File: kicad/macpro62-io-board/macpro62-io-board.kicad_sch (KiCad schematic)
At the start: 387 parts, among them J1 IOB-HS1 MCIO 124 RA <- CB J3, J11 USB-C C1 receptacle vertical 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, J12 USB-C C2 receptacle vertical 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, J13 USB-C C3 receptacle vertical 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, J14 USB-C C4 receptacle vertical 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, J15 USB-C C5 receptacle vertical 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, J16 USB-C C6 receptacle vertical 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, J2 DISPLAY-LINK MCIO 74 RA <- Fa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, J21 USB 3.2 Gen2 Std-A vertical A1, J22 USB 3.2 Gen2 Std-A vertical A2, J23 USB 3.2 Gen2 Std-A vertical A3, J24 USB 3.2 Gen2 Std-A vertical A4, J25 RJ45 vertical magjack 2.5G (E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, J26 DNP rev A: RJ45 10G magjack s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, J27 HDMI type A vertical, J28 Stock audio module connector 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, J29 Speaker 2P JST SH vertical (s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, J3 Stock PSU DC-out 12P (PROVISI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, J30 OPTIONAL 2P: stock I/O-wall b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, J31 I/O-wall flex ZIF 14P 0.5 (st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, J4 Stock PSU signal 6P (PROVISIO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, J5 Micro-Fit 2x4 -> BP J2 (1-2 1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, J6 IOB-LINK GH15 vertical <- BP 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, SW1 Power button PTS810 on the IO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, SW2 DIAG button TL3342 (back side), U1 TPS65994AD PD #1 (C1, C2), U11 TUSB1046A-DCI C1 mux/redriver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, U12 TUSB1046A-DCI C2 mux/redriver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, U13 TUSB1046A-DCI C3 mux/redriver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, U14 TUSB1046A-DCI C4 mux/redriver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, U15 TUSB1046A-DCI C5 mux/redriver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, U16 TUSB1046A-DCI C6 mux/redriver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, U2 TPS65994AD PD #2 (C3, C4), U21 TUSB1002A A1 redriver, U22 TUSB1002A A2 redriver, U23 TUSB1002A A3 redriver, U24 TUSB1002A A4 redriver, U25 SY6280AAC / TPS2553 1.5 A swi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, U26 SY6280AAC / TPS2553 1.5 A swi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, U27 SY6280AAC / TPS2553 1.5 A swi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, U28 SY6280AAC / TPS2553 1.5 A swi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, U3 TPS65994AD PD #3 (C5, C6), U30 DRV5032FB (OD, 5 Hz low power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, U31 DRV5032FB (OD, 5 Hz low power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, U32 CH334R H1b <- H1a port 4, U33 CH334R H2 <- IOB-LINK USB2 (B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, U34 CH334R H1a <- HS1 USB2 (CB PC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, U4 W25Q80DV class 8 Mbit (PD #1 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, U40 TPS259824ONRGER eFuse 12 V (I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, U41 TPS56C215RNNR 5V_C buck 12 A, U42 TPS56C215RNNR 5V_A buck 12 A, U43 TLV62585DRL 3V3 3 A from 5V_A, U50 Intel i226-V 2.5GbE, U51 i226 NVM 2 Mbit+ SPI flash (I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, U6 W25Q80DV class 8 Mbit (PD #2 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, U60 TDP158RSBR HDMI retimer, U61 TLV75511PDBV 1.1 V LDO (TDP15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, U7 W25Q80DV class 8 Mbit (PD #3 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, U70 CM108B USB audio codec (UAC1), U71 PAM8302AAS 2.5 W mono class-D, U80 TLC59116IPWR @0x60 (A3..A0 = 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, U81 LIS2DH12TR @0x18 (optional ro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, U82 BL24C64A-SFRC IOB ID EEPROM @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, U83 TCA9517DGKR I2C buffer: I2C_S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, U84 74LVC1G07 PD_INT_N -> IOB_INT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, Y1 12MHz 3225 +/-20ppm, Y2 12MHz 3225 +/-20ppm, Y3 12MHz 3225 +/-20ppm, Y4 25MHz 3225 +/-30ppm (i226), Y5 12MHz 3225 (CM108B)

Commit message: I/O board: second 2.5GbE (2x i226-V, HR913790A set back), ETH2 plate opening, CPU link pinout v0.2
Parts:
- removed J25: RJ45 vertical magjack 2.5G (ETH1, Xb 63.5), MP62_IO:MP62_RJ45_Mag_2G5_Vertical_PLACEHOLDER, symbol MP62_IO:RJ45_MAG
- removed J26: DNP rev A: RJ45 10G magjack site (rev B AQC107 vi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, MP62_IO:MP62_RJ45_Mag_2G5_Vertical_PLACEHOLDER, symbol MP62_IO:RJ45_MAG
- added C284: 100nF, MP62_IO:C_0402_1005Metric, symbol MP62_IO:C
- added C285: 100nF (CB keeps 1uF + 0.1uF + diode-OR with 3V3_D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, MP62_IO:C_0402_1005Metric, symbol MP62_IO:C
- added C286: dVdt (inrush <= 2 A, value per datasheet), MP62_IO:C_0402_1005Metric, symbol MP62_IO:C
- added C287, C290: 100nF BOOT, MP62_IO:C_0402_1005Metric, symbol MP62_IO:C
- added C288, C291: 4.7uF VREG5, MP62_IO:C_0402_1005Metric, symbol MP62_IO:C
- added C289, C292: SS (value per datasheet), MP62_IO:C_0402_1005Metric, symbol MP62_IO:C
- added C293, C294: 22uF 0805, MP62_IO:C_0402_1005Metric, symbol MP62_IO:C
- added C295: 10uF 0805, MP62_IO:C_0402_1005Metric, symbol MP62_IO:C
- added C296: 10uF 0402, MP62_IO:C_0402_1005Metric, symbol MP62_IO:C
- added J25: HanRun HR913790A vertical 2.5G magjack (ETH1), MP62_IO:MP62_RJ45_HanRun_HR913790A_Vertical_2G5, symbol MP62_IO:RJ45_HR913790A
- added J26: HanRun HR913790A vertical 2.5G magjack (ETH2), MP62_IO:MP62_RJ45_HanRun_HR913790A_Vertical_2G5, symbol MP62_IO:RJ45_HR913790A
- added L45: i226 #2 SVR inductor (value per Intel design guid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, MP62_IO:L_1008_2520Metric, symbol MP62_IO:L
- added R186: FB top (5.10 V), MP62_IO:R_0402_1005Metric, symbol MP62_IO:R
- added R187, R190: FB bottom, MP62_IO:R_0402_1005Metric, symbol MP62_IO:R
- added R188: 10k PG pull-up, MP62_IO:R_0402_1005Metric, symbol MP62_IO:R
- added R189: FB top (3.3 V), MP62_IO:R_0402_1005Metric, symbol MP62_IO:R
- added R191: 10k, MP62_IO:R_0402_1005Metric, symbol MP62_IO:R
- added U52: Intel i226-V 2.5GbE #2 (HS1 k14, PCH RP4 / HSIO 1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, MP62_IO:MP62_Intel_i226V_QFN-56_7x7_P0.4_PLACEHOLDER, symbol MP62_IO:I226V
- added U53: i226 #2 NVM 2 Mbit+ SPI flash (Intel image), MP62_IO:SOIC-8_3.9x4.9mm_P1.27mm, symbol MP62_IO:SPI_FLASH
- added Y6: 25MHz 3225 +/-30ppm (i226 #2), MP62_IO:Crystal_SMD_3225-4Pin_3.2x2.5mm, symbol MP62_IO:XTAL4
- C244, C256: value 10uF 0402 -> 100nF 0402 (magjack common centre tap)
- C245, C246: value 100nF -> 220nF 0201 X7R (i226 TX -> PCH RX AC cap)
- C247: value 10uF 0402 -> 18pF
- C248: value 100nF -> 18pF
- C249: value 22pF -> 22uF 0603
- C250: value 22pF -> 1uF
- C251: value 4.7uF -> 100nF
- C252: value 100nF -> 22uF 0603
- C253: value 10uF 0402 -> 1uF
- C255, C283: value 10uF 0402 -> 100nF
- C257: value 100nF (L into IN+) -> 10uF 0402
- C258: value 100nF (R into IN+, mono sum) -> 100nF
- C259: value 220nF (IN- to AGND) -> 100nF
- C260: value 10uF 0603 -> 10uF 0402
- C261: value 1uF -> 100nF
- C262: value 10uF 1206 25V (header) -> 22pF
- C263: value 100nF (debounce; pull-up on BP) -> 22pF
- C264: value 100nF -> 4.7uF
- C266: value 1uF -> 10uF 0402
- C268, C269: value 100nF -> 10uF 0402
- C270: value 100nF -> 100nF (L into IN+)
- C271: value 100nF -> 100nF (R into IN+, mono sum)
- C272: value 100nF (CB keeps 1uF + 0.1uF + diode-OR with 3V3_DSW) -> 220nF (IN- to AGND)
- C273: value dVdt (inrush <= 2 A, value per datasheet) -> 10uF 0603
- C274: value 100nF BOOT -> 1uF
- C275: value 4.7uF VREG5 -> 10uF 1206 25V (header)
- C276: value SS (value per datasheet) -> 100nF (debounce; pull-up on BP)
- C277: value 100nF BOOT -> 100nF
- C278: value 4.7uF VREG5 -> 100nF
- C279: value SS (value per datasheet) -> 1uF
- C280, C281: value 22uF 0805 -> 100nF
- C282: value 10uF 0805 -> 100nF
- L44: value i226 SVR inductor (value per Intel design guide) -> i226 #1 SVR inductor (value per Intel design guide)
- R132: value 10k (DNP if CB pulls up) -> 330R (green link LED; orange half of the bicolour unused); now fitted; now in the parts list
- R133: value 1.8k DDC pull-up (sink side) -> 330R (yellow activity LED)
- R134: value 1.8k DDC pull-up (sink side) -> 10k (DNP if CB pulls up); now not fitted; now left out of the parts list
- R135: value 100k HPD pull-down -> RSET (value per Intel)
- R136: value 100k -> 330R (green link LED; orange half of the bicolour unused)
- R137: value 10k (L+R mix into the mono ADC; CM6646 upgrade = stereo line in) -> 330R (yellow activity LED)
- R138: value 10k -> 10k (DNP if CB pulls up); now not fitted; now left out of the parts list
- R139: value DNP 2.2k (only if the stock line-in jack is a mic/combo) -> 1.8k DDC pull-up (sink side); now fitted; now in the parts list
- R140: value 100k jack-detect pull-up -> 1.8k DDC pull-up (sink side)
- R141: value 100k jack-detect pull-up -> 100k HPD pull-down
- R142: value 0R (optical TX/RX module supply; 10R if the module wants filtering) -> 100k
- R143: value DNP: optical input not supported by CM108B (CM6646 upgrade) -> 10k (L+R mix into the mono ADC; CM6646 upgrade = stereo line in); now fitted; now in the parts list
- R144: value 100k (amp off until codec GPIO3 enables; firmware mutes on JD_HP) -> 10k
- R145: value DNP 0R (only if J4 5/6 prove to be 3.3 V SMBus) -> DNP 2.2k (only if the stock line-in jack is a mic/combo)
- R146: value DNP 0R -> 100k jack-detect pull-up; now fitted; now in the parts list
- R147: value DNP 0R: GND? (probe) -> 100k jack-detect pull-up; now fitted; now in the parts list
- R148: value DNP 0R: GND? (probe) -> 0R (optical TX/RX module supply; 10R if the module wants filtering); now fitted; now in the parts list
- R149: value 0R: community claim pins 3+6 = power button -> DNP: optical input not supported by CM108B (CM6646 upgrade); now not fitted; now left out of the parts list
- R150: value DNP 0R: LED-MCU logic 3V3? (probe) -> 100k (amp off until codec GPIO3 enables; firmware mutes on JD_HP); now fitted; now in the parts list
- R151: value DNP 0R: 3V3? (probe) -> DNP 0R (only if J4 5/6 prove to be 3.3 V SMBus)
- R152: value 0R: button return (pins 3+6) -> DNP 0R; now not fitted; now left out of the parts list
- R153: value DNP 0R: LED-MCU I2C SCL? (probe; must be 3.3 V) -> DNP 0R: GND? (probe)
- R154: value DNP 0R: LED-MCU I2C SDA? (probe) -> DNP 0R: GND? (probe)
- R155: value DNP 0R: flex IRQ/motion? (probe) -> 0R: community claim pins 3+6 = power button; now fitted; now in the parts list
- R156: value DNP 0R: LED supply 5 V? (probe; S0 only) -> DNP 0R: LED-MCU logic 3V3? (probe)
- R157: value DNP 0R: GND? (probe) -> DNP 0R: 3V3? (probe)
- R158: value DNP 0R: 3V3? (probe) -> 0R: button return (pins 3+6); now fitted; now in the parts list
- R159: value DNP 0R: GND? (probe) -> DNP 0R: LED-MCU I2C SCL? (probe; must be 3.3 V)
- R160: value DNP 0R: GND? (probe) -> DNP 0R: LED-MCU I2C SDA? (probe)
- R161: value 10k (read via PD #1 GPIO2; S0 only) -> DNP 0R: flex IRQ/motion? (probe); now not fitted; now left out of the parts list
- R162: value REXT ~ 2.7k (Iout ~ 7 mA max; PWM per channel) -> DNP 0R: LED supply 5 V? (probe; S0 only); now not fitted; now left out of the parts list
- R163: value 10k (write-protect by default) -> DNP 0R: GND? (probe); now not fitted; now left out of the parts list
- R164: value DNP 0R (program) -> DNP 0R: 3V3? (probe)
- R165, R166: value 4.7k -> DNP 0R: GND? (probe); now not fitted; now left out of the parts list
- R167: value 10k (DNP if the BP pulls up) -> 10k (read via PD #1 GPIO2; S0 only); now fitted; now in the parts list
- R168: value UVLO top (~10.5 V on) -> REXT ~ 2.7k (Iout ~ 7 mA max; PWM per channel)
- R169: value UVLO bottom -> 10k (write-protect by default)
- R170: value ILIM ~10 A (value per datasheet) -> DNP 0R (program); now not fitted; now left out of the parts list
- R171: value IMON (value per datasheet) -> 4.7k
- R172: value 10k -> 4.7k
- R173: value 10k -> 10k (DNP if the BP pulls up); now not fitted; now left out of the parts list
- R174: value 0R (fault -> IOB_INT_N, OD) -> UVLO top (~10.5 V on)
- R175: value MODE strap (FCCM, 800 kHz) -> UVLO bottom
- R176: value FB top (5.10 V) -> ILIM ~10 A (value per datasheet)
- R177: value FB bottom -> IMON (value per datasheet)
- R178: value 10k PG pull-up -> 10k
- R179: value MODE strap (FCCM, 800 kHz) -> 10k
- R180: value FB top (5.10 V) -> 0R (fault -> IOB_INT_N, OD)
- R181: value FB bottom -> MODE strap (FCCM, 800 kHz)
- R182: value 10k PG pull-up -> FB top (5.10 V)
- R183: value FB top (3.3 V) -> FB bottom
- R184: value FB bottom -> 10k PG pull-up
- R185: value 10k -> MODE strap (FCCM, 800 kHz)
- U50: value Intel i226-V 2.5GbE -> Intel i226-V 2.5GbE #1 (HS1 k10, PCH RP3 / HSIO 12, CLKOUT_SRC12)
- U51: value i226 NVM 2 Mbit+ SPI flash (Intel image) -> i226 #1 NVM 2 Mbit+ SPI flash (Intel image)
- Y4: value 25MHz 3225 +/-30ppm (i226) -> 25MHz 3225 +/-30ppm (i226 #1)
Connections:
- net +12V_MAIN: now also C275.1, R174.1; no longer C262.1, R168.1
- net 1V1_HDMI: now also C257.1, C258.1, C259.1; no longer C244.1, C245.1, C246.1
- net 3V3: now also C252.1, C253.1, C254.1, C255.1, C260.1, C261.1, R133.2, R134.2, R136.2, R137.2, R138.2, R148.1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; no longer C247.1, C248.1, C271.1, C280.1, C281.1, R142.1, R158.2, R161.2, R165.2, R166.2, R183.1
- net 3V3_SB: now also C277.1, C278.1, C279.1, C280.1, C281.1, C282.1, R156.2, R157.2, R169.2, R179.2, R184.2, C296.1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; no longer C264.1, C265.1, C266.1, C267.1, C268.1, C269.1, C270.1, R150.2, R151.2, R163.2, R167.2, R172.2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
- net 5V_A: now also C268.1, C273.1, C274.1, R162.2, C295.1, R186.1; no longer C255.1, C260.1, C261.1, C282.1, R156.2, R180.1
- net 5V_C: now also R182.1; no longer R176.1
- net AGND: now also C272.2; no longer C259.2
- net AMP_INN: now also C272.1; no longer C259.1
- net AMP_INP: now also C270.2, C271.2; no longer C257.2, C258.2
- net AMP_SD#: now also R150.1; no longer R144.1
- net AUD_3V3: now also C264.1, C265.1, R146.2, R147.2; no longer C251.1, C252.1, R140.2, R141.2
- net AUD_AVDD: now also C266.1, C267.1; no longer C253.1, C254.1
- net AUD_OPT_3V3: now also C269.1, R148.2; no longer C256.1, R142.2
- net AUD_XI: now also C262.1; no longer C249.1
- net AUD_XO: now also C263.1; no longer C250.1
- net BK3_FB: now also R189.2, R190.1; no longer R183.2, R184.1
- net BKA_BOOT: now also C290.1; no longer C277.1
- net BKA_FB: now also R186.2, R187.1; no longer R180.2, R181.1
- net BKA_MODE: now also R185.1; no longer R179.1
- net BKA_SS: now also C292.1; no longer C279.1
- net BKA_SW: now also C290.2; no longer C277.2
- net BKA_VREG5: now also C291.1; no longer C278.1
- net BKC_BOOT: now also C287.1; no longer C274.1
- net BKC_FB: now also R182.2, R183.1; no longer R176.2, R177.1
- net BKC_MODE: now also R181.1; no longer R175.1
- net BKC_SS: now also C289.1; no longer C276.1
- net BKC_SW: now also C287.2; no longer C274.2
- net BKC_VREG5: now also C288.1; no longer C275.1
- net DIAG_BTN_N: now also R167.1; no longer R161.1
- net DL_HPD2: now also R142.1; no longer R136.1
- net EFUSE_DVDT: now also C286.1; no longer C273.1
- net EFUSE_EN: now also R174.2, R175.1; no longer R168.2, R169.1
- net EFUSE_FLT#: now also R179.1, R180.1; no longer R173.1, R174.1
- net EFUSE_ILIM: now also R176.1; no longer R170.1
- net EFUSE_IMON: now also R177.1; no longer R171.1
- net EFUSE_PG: now also R178.1; no longer R172.1
- net ETH1_LED_ACT#: now also J25.13 (LEDY_K)
- net ETH1_LED_LINK#: now also J25.11 (LEDGO_11)
- net ETH1_MDI0_N: now also J25.3 (TRD1-)
- net ETH1_MDI0_P: now also J25.2 (TRD1+)
- net ETH1_MDI1_N: now also J25.5 (TRD2-)
- net ETH1_MDI1_P: now also J25.4 (TRD2+)
- net ETH1_MDI2_N: now also J25.7 (TRD3-)
- net ETH1_MDI2_P: now also J25.6 (TRD3+)
- net ETH1_MDI3_N: now also J25.9 (TRD4-)
- net ETH1_MDI3_P: now also J25.8 (TRD4+)
- net GND: now also C257.2, C258.2, C259.2, C274.2, C277.2, R141.2, R142.2, R149.2, R150.2, R153.2, R154.2, R158.2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; no longer C245.2, C246.2, C270.2, C271.2, C272.2, R136.2, R143.2, R144.2, R147.2, R148.2, R152.2, R157.2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
- net HDMI_5V_OUT: now also R139.2, R140.2; no longer R133.2, R134.2
- net HDMI_HPD: now also R141.1; no longer R135.1
- net HDMI_SCL: now also R139.1; no longer R133.1
- net HDMI_SDA: now also R140.1; no longer R134.1
- net HP_L: now also C270.1; no longer C257.1
- net HP_R: now also C271.1; no longer C258.1
- net I226_CLKREQ#: now also R134.1; no longer R132.1
- net I226_PERST#: now also U52.7 (PERST#)
- net I226_WAKE#: now also U52.9 (WAKE#)
- net I2C_PD_SCL: now also R171.1; no longer R165.1
- net I2C_PD_SDA: now also R172.1; no longer R166.1
- net I2C_SYS_SCL: now also R151.2, R159.2; no longer R145.2, R153.2
- net I2C_SYS_SDA: now also R152.2, R160.2; no longer R146.2, R154.2
- net IOB_EE_WP: now also R169.1, R170.1; no longer R163.1, R164.1
- net IOB_INT_N: now also R161.2, R173.1, R180.2; no longer R155.2, R167.1, R174.2
- net JD_HP: now also R146.1; no longer R140.1
- net JD_LINE: now also R147.1; no longer R141.1
- net LED_REXT: now also R168.1; no longer R162.1
- net LINE_IN_MONO: now also R143.2, R144.2, R145.2; no longer R137.2, R138.2, R139.2
- net LINE_L: now also R143.1; no longer R137.1
- net LINE_R: now also R144.1; no longer R138.1
- net MIC_BIAS: now also R145.1; no longer R139.1
- net PG_3V3: now also R191.1; no longer R185.1
- net PG_5VA: now also R188.1; no longer R182.1
- net PG_5VC: now also R184.1; no longer R178.1
- net PSU_SMB_CLK: now also R151.1; no longer R145.1
- net PSU_SMB_DAT: now also R152.1; no longer R146.1
- net PWRBTN_IN_N: now also C276.1, R155.2; no longer C263.1, R149.2
- net SPDIF_RX: now also R149.1; no longer R143.1
- net VBAT_RTC: now also C285.1; no longer C272.1
- net WALL_P1: now also R153.1; no longer R147.1
- net WALL_P10: now also R162.1; no longer R156.1
- net WALL_P11: now also R163.1; no longer R157.1
- net WALL_P12: now also R164.1; no longer R158.1
- net WALL_P13: now also R165.1; no longer R159.1
- net WALL_P14: now also R166.1; no longer R160.1
- net WALL_P2: now also R154.1; no longer R148.1
- net WALL_P3: now also R155.1; no longer R149.1
- new net ETH1_CT: C244.1, J25.1 (CT)
- new net ETH1_LEDG_A: J25.12 (LEDGO_12), R132.1
- new net ETH1_LEDY_A: J25.14 (LEDY_A), R133.1
- new net ETH2_CT: C256.1, J26.1 (CT)
- new net ETH2_LEDG_A: J26.12 (LEDGO_12), R136.1
- new net ETH2_LEDY_A: J26.14 (LEDY_A), R137.1
- new net ETH2_LED_ACT#: J26.13 (LEDY_K), U52.29 (LED1#)
- new net ETH2_LED_LINK#: J26.11 (LEDGO_11), U52.28 (LED0#)
- new net ETH2_MDI0_N: J26.3 (TRD1-), U52.21 (MDI0N)
- new net ETH2_MDI0_P: J26.2 (TRD1+), U52.20 (MDI0P)
- new net ETH2_MDI1_N: J26.5 (TRD2-), U52.23 (MDI1N)
- new net ETH2_MDI1_P: J26.4 (TRD2+), U52.22 (MDI1P)
- new net ETH2_MDI2_N: J26.7 (TRD3-), U52.25 (MDI2N)
- new net ETH2_MDI2_P: J26.6 (TRD3+), U52.24 (MDI2P)
- new net ETH2_MDI3_N: J26.9 (TRD4-), U52.27 (MDI3N)
- new net ETH2_MDI3_P: J26.8 (TRD4+), U52.26 (MDI3P)
- new net I226B_0V9: C249.1, C250.1, C251.1, L45.2, U52.18 (VCC0P9)
- new net I226B_RSET: R135.1, U52.31 (RSET)
- new net I226B_SPI_CLK: U52.13 (SPI_CLK), U53.6 (CLK)
- new net I226B_SPI_CS#: U52.12 (SPI_CS#), U53.1 (CS#)
- new net I226B_SPI_MISO: U52.15 (SPI_MISO), U53.2 (DO)
- new net I226B_SPI_MOSI: U52.14 (SPI_MOSI), U53.5 (DI)
- new net I226B_SVR: L45.1, U52.17 (SVR_SW)
- new net I226B_XI: C247.1, U52.10 (XTAL1), Y6.1 (X1)
- new net I226B_XO: C248.1, U52.11 (XTAL2), Y6.3 (X2)
- new net PCIE_I226B_RXC_N: C246.2, J1.B58 (PCIE_I226B_RX_N)
- new net PCIE_I226B_RXC_P: C245.2, J1.B57 (PCIE_I226B_RX_P)
- new net PCIE_I226B_RX_N: C246.1, U52.2 (PETN)
- new net PCIE_I226B_RX_P: C245.1, U52.1 (PETP)
- new net PCIE_I226B_TX_N: J1.A58 (PCIE_I226B_TX_N), U52.4 (PERN)
- new net PCIE_I226B_TX_P: J1.A57 (PCIE_I226B_TX_P), U52.3 (PERP)
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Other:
- note added: "Ethernet: 2 x i226-V (U50 -> J25 ETH1, U52 -> J26 ETH2), D-IO2 resolved 2026-10-02"
- note removed: "Ethernet: i226-V U50 -> J25; J26 DNP site (rev B AQC107)"

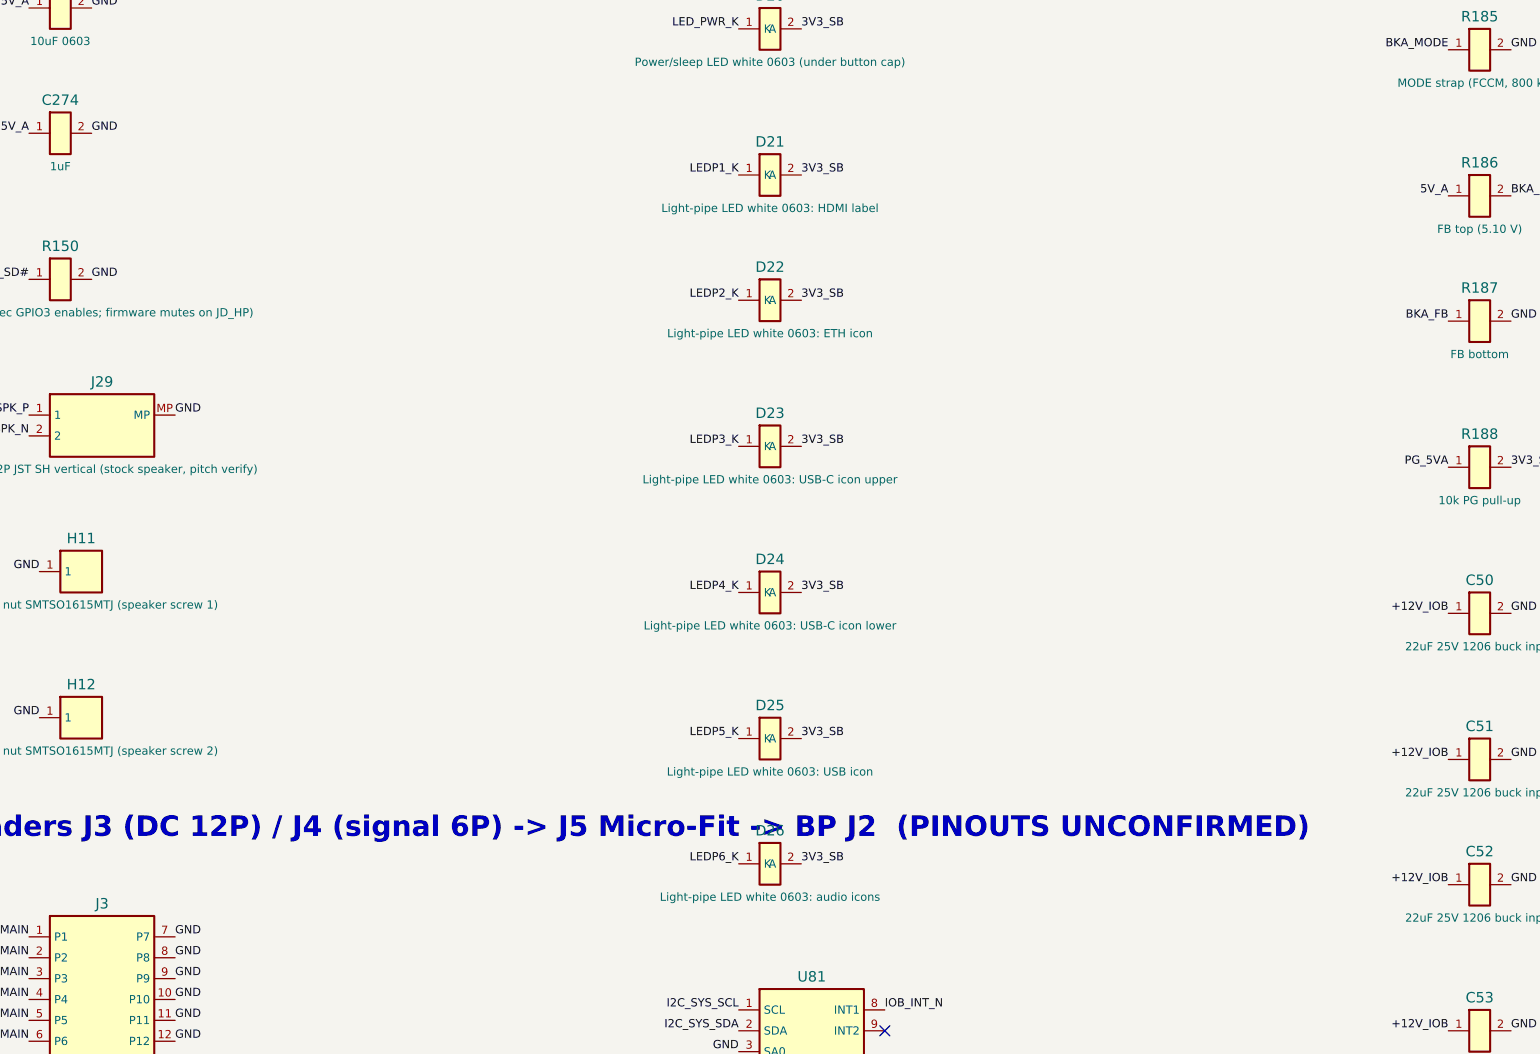
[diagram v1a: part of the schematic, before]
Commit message: I/O plate v2: curved inner face, 821-2222 flex seat + trace, flex-LED lighting, foam insulator DXF
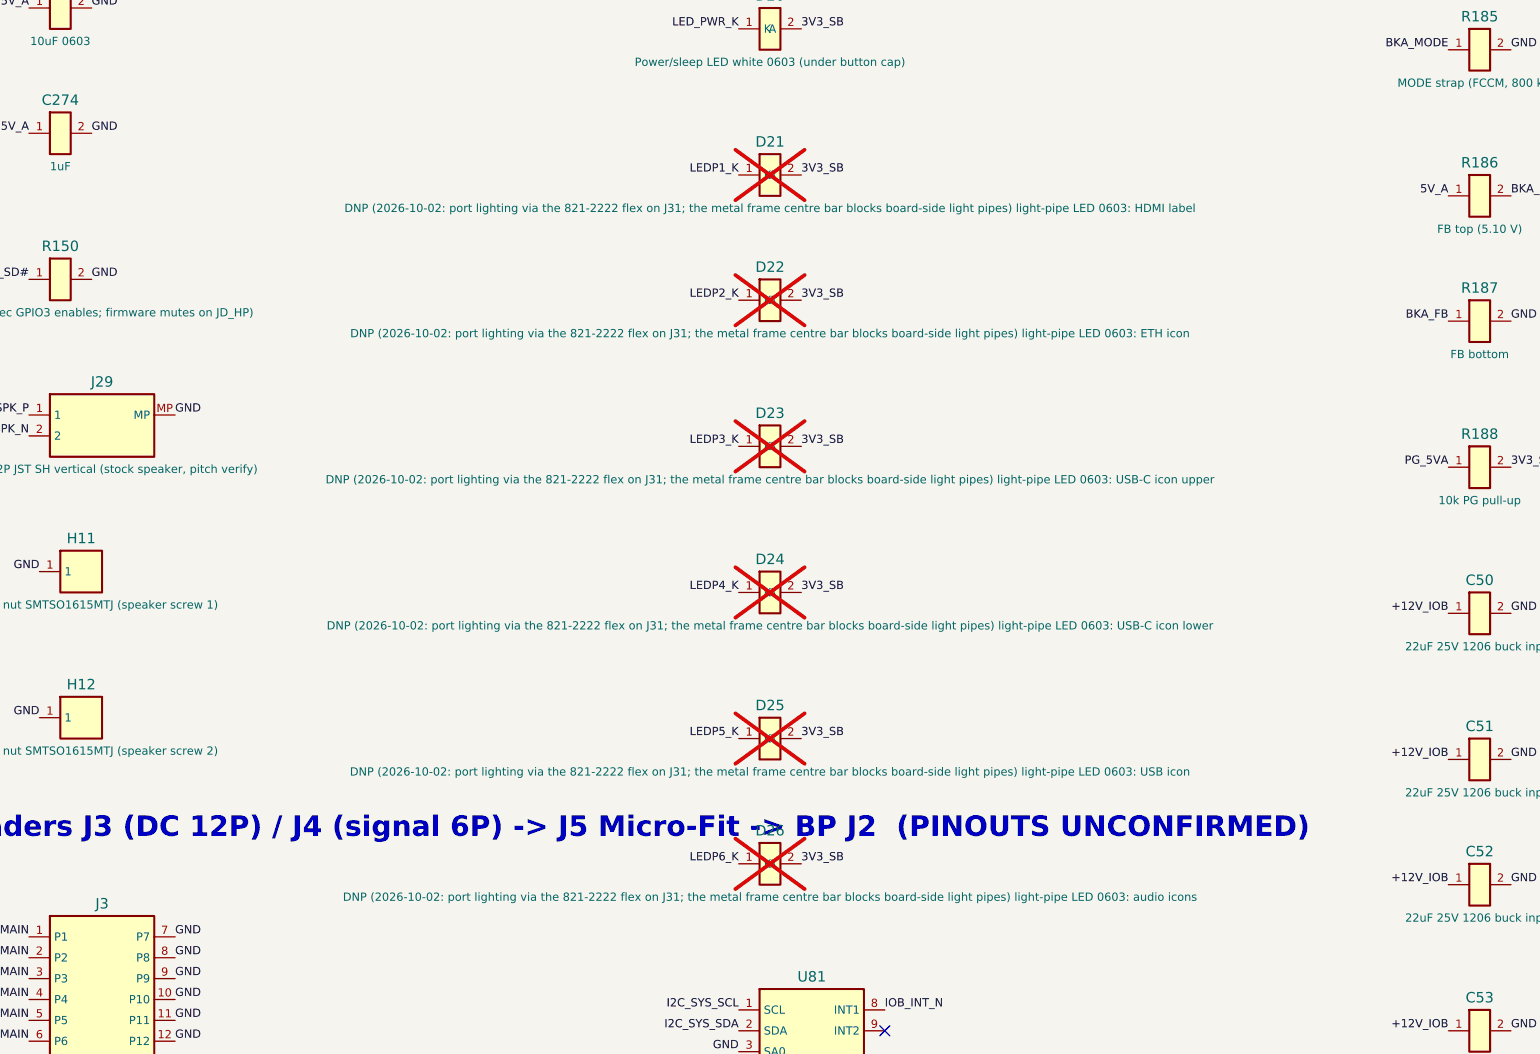
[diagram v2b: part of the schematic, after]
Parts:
- D21: value Light-pipe LED white 0603: HDMI label -> DNP (2026-10-02: port lighting via the 821-2222 flex on J31; the metal frame centre bar blocks board-side light pipes) 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; now not fitted; now left out of the parts list
- D22: value Light-pipe LED white 0603: ETH icon -> DNP (2026-10-02: port lighting via the 821-2222 flex on J31; the metal frame centre bar blocks board-side light pipes) 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; now not fitted; now left out of the parts list
- D23: value Light-pipe LED white 0603: USB-C icon upper -> DNP (2026-10-02: port lighting via the 821-2222 flex on J31; the metal frame centre bar blocks board-side light pipes) 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; now not fitted; now left out of the parts list
- D24: value Light-pipe LED white 0603: USB-C icon lower -> DNP (2026-10-02: port lighting via the 821-2222 flex on J31; the metal frame centre bar blocks board-side light pipes) 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; now not fitted; now left out of the parts list
- D25: value Light-pipe LED white 0603: USB icon -> DNP (2026-10-02: port lighting via the 821-2222 flex on J31; the metal frame centre bar blocks board-side light pipes) 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; now not fitted; now left out of the parts list
- D26: value Light-pipe LED white 0603: audio icons -> DNP (2026-10-02: port lighting via the 821-2222 flex on J31; the metal frame centre bar blocks board-side light pipes) 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; now not fitted; now left out of the parts list

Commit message: I/O: tilted port risers (USB-C/USB-A/HDMI, DF40 + flex jumpers), low RJ45 + V24P05S magnetics, fan+AirPort CONN_C at stock position, ASM1182e lane share; plate R=111
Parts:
- removed J25: HanRun HR913790A vertical 2.5G magjack (ETH1), MP62_IO:MP62_RJ45_HanRun_HR913790A_Vertical_2G5, symbol MP62_IO:RJ45_HR913790A
- removed J26: HanRun HR913790A vertical 2.5G magjack (ETH2), MP62_IO:MP62_RJ45_HanRun_HR913790A_Vertical_2G5, symbol MP62_IO:RJ45_HR913790A
- added C297, C298, C300, C301, C302, C303, C304: 100nF, MP62_IO:C_0402_1005Metric, symbol MP62_IO:C
- added C299: 1uF, MP62_IO:C_0402_1005Metric, symbol MP62_IO:C
- added C305: 100nF (CB keeps 1uF + 0.1uF + diode-OR with 3V3_D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, MP62_IO:C_0402_1005Metric, symbol MP62_IO:C
- added C306: dVdt (inrush <= 2 A, value per datasheet), MP62_IO:C_0402_1005Metric, symbol MP62_IO:C
- added C307, C310: 100nF BOOT, MP62_IO:C_0402_1005Metric, symbol MP62_IO:C
- added C308, C311: 4.7uF VREG5, MP62_IO:C_0402_1005Metric, symbol MP62_IO:C
- added C309, C312: SS (value per datasheet), MP62_IO:C_0402_1005Metric, symbol MP62_IO:C
- added C313, C314: 22uF 0805, MP62_IO:C_0402_1005Metric, symbol MP62_IO:C
- added C315: 10uF 0805, MP62_IO:C_0402_1005Metric, symbol MP62_IO:C
- added C316: 10uF 0402, MP62_IO:C_0402_1005Metric, symbol MP62_IO:C
- added F90: 1.5 A PTC / 0R fuse link (+12V_IOB -> FAN_12V), MP62_IO:R_0402_1005Metric, symbol MP62_IO:R
- added J25: Non-magnetic vertical RJ45 (ETH1) C55547809, MP62_IO:MP62_RJ45_Vertical_SMD_NoMag_PLACEHOLDER, symbol MP62_IO:RJ45_NOMAG
- added J26: Non-magnetic vertical RJ45 (ETH2) C55547809, MP62_IO:MP62_RJ45_Vertical_SMD_NoMag_PLACEHOLDER, symbol MP62_IO:RJ45_NOMAG
- added J7: CONN_C fan + AirPort (stock press B2B, 2x20 @0.5;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, MP62_IO:MP62_Hirose_DF12-40DS-0.5V_PLACEHOLDER, symbol MP62_IO:CONNC_40
- added Q90: MMBT3904 remote diode (or omit: EMC2101 internal 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, MP62_IO:C_0402_1005Metric, symbol MP62_IO:C
- added R192, R204: 10k, MP62_IO:R_0402_1005Metric, symbol MP62_IO:R
- added R193: 0R (fault -> IOB_INT_N, OD), MP62_IO:R_0402_1005Metric, symbol MP62_IO:R
- added R194, R198: MODE strap (FCCM, 800 kHz), MP62_IO:R_0402_1005Metric, symbol MP62_IO:R
- added R195, R199: FB top (5.10 V), MP62_IO:R_0402_1005Metric, symbol MP62_IO:R
- added R196, R200, R203: FB bottom, MP62_IO:R_0402_1005Metric, symbol MP62_IO:R
- added R197, R201: 10k PG pull-up, MP62_IO:R_0402_1005Metric, symbol MP62_IO:R
- added R202: FB top (3.3 V), MP62_IO:R_0402_1005Metric, symbol MP62_IO:R
- added T1: JASN V24P05S 2.5G magnetics (ETH1), C2827281, MP62_IO:MP62_JASN_V24P05S_SMD-24P_15.1x7.1_PLACEHOLDER, symbol MP62_IO:V24P05S
- added T2: JASN V24P05S 2.5G magnetics (ETH2), C2827281, MP62_IO:MP62_JASN_V24P05S_SMD-24P_15.1x7.1_PLACEHOLDER, symbol MP62_IO:V24P05S
- added U35: CH334R H3 <- H2 port 4 (A4 + AirPort Bluetooth + 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, MP62_IO:MP62_WCH_CH334R_QFN-24_4x4_P0.5_PLACEHOLDER, symbol MP62_IO:CH334R
- added U90: EMC2101 fan controller (SMBus 0x4C, PWM 25 kHz, T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, MP62_IO:MSOP-8_3x3mm_P0.65mm, symbol MP62_IO:EMC2101
- added U91: ASM1182e PCIe Gen2 switch: up = HS1 k14 (PCH RP4)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, MP62_IO:MP62_ASMedia_ASM1182e_QFN-64_9x9_P0.5_PLACEHOLDER, symbol MP62_IO:ASM1182E
- added U92: 3V3 WLAN load switch (TPS22918 class, 2 A) 3V3 ->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, MP62_IO:C_0402_1005Metric, symbol MP62_IO:C
- added Y7: 12MHz 3225 +/-20ppm, MP62_IO:Crystal_SMD_3225-4Pin_3.2x2.5mm, symbol MP62_IO:XTAL4
- added Y8: 25MHz 3225 (ASM1182e, per datasheet), MP62_IO:Crystal_SMD_3225-4Pin_3.2x2.5mm, symbol MP62_IO:XTAL4
- C233, C234: value 220nF 0201 X7R (i226 TX -> PCH RX AC cap) -> 22pF
- C235, C236: value 18pF -> 1uF
- C237: value 22uF 0603 -> 220nF 0201 X7R (i226 TX -> PCH RX AC cap)
- C238, C250: value 1uF -> 220nF 0201 X7R (i226 TX -> PCH RX AC cap)
- C239: value 100nF -> 18pF
- C240, C252: value 22uF 0603 -> 18pF
- C241: value 1uF -> 22uF 0603
- C242, C255, C258: value 100nF -> 1uF
- C244: value 100nF 0402 (magjack common centre tap) -> 22uF 0603
- C245: value 220nF 0201 X7R (i226 TX -> PCH RX AC cap) -> 1uF
- C246: value 220nF 0201 X7R (i226 TX -> PCH RX AC cap) -> 100nF
- C247: value 18pF -> 100nF
- C248: value 18pF -> 100nF 0402 (chip-side centre taps, i226 MDI)
- C249: value 22uF 0603 -> 1nF 2 kV 1206 (Bob-Smith to chassis)
- C251: value 100nF -> 220nF 0201 X7R (i226 TX -> PCH RX AC cap)
- C253: value 1uF -> 18pF
- C254: value 100nF -> 22uF 0603
- C256: value 100nF 0402 (magjack common centre tap) -> 100nF
- C257: value 10uF 0402 -> 22uF 0603
- C260, C269: value 10uF 0402 -> 100nF
- C261: value 100nF -> 100nF 0402 (chip-side centre taps, i226 MDI)
- C262: value 22pF -> 1nF 2 kV 1206 (Bob-Smith to chassis)
- C263: value 22pF -> 220nF 0201 (switch TX -> PCH RX AC cap)
- C264: value 4.7uF -> 220nF 0201 (switch TX -> PCH RX AC cap)
- C265: value 100nF -> 100nF 0201 (switch TX -> AirPort RX AC cap)
- C266: value 10uF 0402 -> 100nF 0201 (switch TX -> AirPort RX AC cap)
- C267: value 100nF -> 10uF
- C268: value 10uF 0402 -> 1uF
- C270: value 100nF (L into IN+) -> 10uF
- C271: value 100nF (R into IN+, mono sum) -> 100nF
- C272: value 220nF (IN- to AGND) -> 100nF
- C273: value 10uF 0603 -> 22uF 0805
- C275: value 10uF 1206 25V (header) -> 100nF
- C276: value 100nF (debounce; pull-up on BP) -> 10uF 25V 0805
- C277, C280: value 100nF -> 10uF 0402
- C279: value 1uF -> 100nF
- C282, C283: value 100nF -> 22pF
- C284: value 100nF -> 4.7uF
- C285: value 100nF (CB keeps 1uF + 0.1uF + diode-OR with 3V3_DSW) -> 100nF
- C286: value dVdt (inrush <= 2 A, value per datasheet) -> 10uF 0402
- C287: value 100nF BOOT -> 100nF
- C288: value 4.7uF VREG5 -> 10uF 0402
- C289: value SS (value per datasheet) -> 10uF 0402
- C290: value 100nF BOOT -> 100nF (L into IN+)
- C291: value 4.7uF VREG5 -> 100nF (R into IN+, mono sum)
- C292: value SS (value per datasheet) -> 220nF (IN- to AGND)
- C293: value 22uF 0805 -> 10uF 0603
- C294: value 22uF 0805 -> 1uF
- C295: value 10uF 0805 -> 10uF 1206 25V (header)
- C296: value 10uF 0402 -> 100nF (debounce; pull-up on BP)
- R132: value 330R (green link LED; orange half of the bicolour unused) -> 75R 0402 (Bob-Smith)
- R133: value 330R (yellow activity LED) -> 75R 0402 (Bob-Smith)
- R134, R138: value 10k (DNP if CB pulls up) -> 75R 0402 (Bob-Smith); now fitted; now in the parts list
- R135: value RSET (value per Intel) -> 75R 0402 (Bob-Smith)
- R136: value 330R (green link LED; orange half of the bicolour unused) -> 10k (DNP if CB pulls up); now not fitted; now left out of the parts list
- R137: value 330R (yellow activity LED) -> RSET (value per Intel)
- R139, R140: value 1.8k DDC pull-up (sink side) -> 75R 0402 (Bob-Smith)
- R141: value 100k HPD pull-down -> 75R 0402 (Bob-Smith)
- R142: value 100k -> 10k (DNP if CB pulls up); now not fitted; now left out of the parts list
- R143: value 10k (L+R mix into the mono ADC; CM6646 upgrade = stereo line in) -> 0R: HS1 CLKREQ# for RP4 held low (switch upstream needs REFCLK always)
- R144: value 10k -> 10k TACH pull-up
- R145: value DNP 2.2k (only if the stock line-in jack is a mic/combo) -> 4k7 PWM pull-up (open-drain); now fitted; now in the parts list
- R146: value 100k jack-detect pull-up -> 10k (radio on; drive from TLC59116/IOB GPIO if wanted)
- R147: value 100k jack-detect pull-up -> 10k
- R148: value 0R (optical TX/RX module supply; 10R if the module wants filtering) -> 10k
- R149: value DNP: optical input not supported by CM108B (CM6646 upgrade) -> 0R (3V3_SB alias: confirm the stock rail on M-IOC1); now fitted; now in the parts list
- R150: value 100k (amp off until codec GPIO3 enables; firmware mutes on JD_HP) -> 0R DNP (fan-assembly SMBus, if present); now not fitted; now left out of the parts list
- R151: value DNP 0R (only if J4 5/6 prove to be 3.3 V SMBus) -> 0R DNP
- R152: value DNP 0R -> 1.8k DDC pull-up (sink side); now fitted; now in the parts list
- R153: value DNP 0R: GND? (probe) -> 1.8k DDC pull-up (sink side); now fitted; now in the parts list
- R154: value DNP 0R: GND? (probe) -> 100k HPD pull-down; now fitted; now in the parts list
- R155: value 0R: community claim pins 3+6 = power button -> 100k
- R156: value DNP 0R: LED-MCU logic 3V3? (probe) -> 10k (L+R mix into the mono ADC; CM6646 upgrade = stereo line in); now fitted; now in the parts list
- R157: value DNP 0R: 3V3? (probe) -> 10k; now fitted; now in the parts list
- R158: value 0R: button return (pins 3+6) -> DNP 2.2k (only if the stock line-in jack is a mic/combo); now not fitted; now left out of the parts list
- R159: value DNP 0R: LED-MCU I2C SCL? (probe; must be 3.3 V) -> 100k jack-detect pull-up; now fitted; now in the parts list
- R160: value DNP 0R: LED-MCU I2C SDA? (probe) -> 100k jack-detect pull-up; now fitted; now in the parts list
- R161: value DNP 0R: flex IRQ/motion? (probe) -> 0R (optical TX/RX module supply; 10R if the module wants filtering); now fitted; now in the parts list
- R162: value DNP 0R: LED supply 5 V? (probe; S0 only) -> DNP: optical input not supported by CM108B (CM6646 upgrade)
- R163: value DNP 0R: GND? (probe) -> 100k (amp off until codec GPIO3 enables; firmware mutes on JD_HP); now fitted; now in the parts list
- R164: value DNP 0R: 3V3? (probe) -> DNP 0R (only if J4 5/6 prove to be 3.3 V SMBus)
- R165: value DNP 0R: GND? (probe) -> DNP 0R
- R167: value 10k (read via PD #1 GPIO2; S0 only) -> DNP 0R: GND? (probe); now not fitted; now left out of the parts list
- R168: value REXT ~ 2.7k (Iout ~ 7 mA max; PWM per channel) -> 0R: community claim pins 3+6 = power button
- R169: value 10k (write-protect by default) -> DNP 0R: LED-MCU logic 3V3? (probe); now not fitted; now left out of the parts list
- R170: value DNP 0R (program) -> DNP 0R: 3V3? (probe)
- R171: value 4.7k -> 0R: button return (pins 3+6)
- R172: value 4.7k -> DNP 0R: LED-MCU I2C SCL? (probe; must be 3.3 V); now not fitted; now left out of the parts list
- R173: value 10k (DNP if the BP pulls up) -> DNP 0R: LED-MCU I2C SDA? (probe)
- R174: value UVLO top (~10.5 V on) -> DNP 0R: flex IRQ/motion? (probe); now not fitted; now left out of the parts list
- R175: value UVLO bottom -> DNP 0R: LED supply 5 V? (probe; S0 only); now not fitted; now left out of the parts list
- R176: value ILIM ~10 A (value per datasheet) -> DNP 0R: GND? (probe); now not fitted; now left out of the parts list
- R177: value IMON (value per datasheet) -> DNP 0R: 3V3? (probe); now not fitted; now left out of the parts list
- R178, R179: value 10k -> DNP 0R: GND? (probe); now not fitted; now left out of the parts list
- R180: value 0R (fault -> IOB_INT_N, OD) -> 10k (read via PD #1 GPIO2; S0 only)
- R181: value MODE strap (FCCM, 800 kHz) -> REXT ~ 2.7k (Iout ~ 7 mA max; PWM per channel)
- R182: value FB top (5.10 V) -> 10k (write-protect by default)
- R183: value FB bottom -> DNP 0R (program); now not fitted; now left out of the parts list
- R184: value 10k PG pull-up -> 4.7k
- R185: value MODE strap (FCCM, 800 kHz) -> 4.7k
- R186: value FB top (5.10 V) -> 10k (DNP if the BP pulls up); now not fitted; now left out of the parts list
- R187: value FB bottom -> UVLO top (~10.5 V on)
- R188: value 10k PG pull-up -> UVLO bottom
- R189: value FB top (3.3 V) -> ILIM ~10 A (value per datasheet)
- R190: value FB bottom -> IMON (value per datasheet)
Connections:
- net ETH2_LEDG_A is gone; now on net I226_CLKREQ#: R136.1
- net +12V_IOB: now also F90.1
- net +12V_MAIN: now also C295.1, R187.1; no longer C275.1, R174.1
- net 1V1_HDMI: now also C277.1, C278.1, C279.1; no longer C257.1, C258.1, C259.1
- net 3V3: now also C244.1, C245.1, C246.1, C247.1, C257.1, C258.1, C259.1, C270.1, C271.1, C272.1, C280.1, C281.1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; no longer C240.1, C241.1, C242.1, C243.1, C252.1, C253.1, C254.1, C255.1, C261.1, C284.1, C293.1, C294.1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
- net 3V3_SB: now also R149.1, R170.2, R182.2, R186.2, C297.1, C298.1, C299.1, C300.1, C301.1, C302.1, C303.1, C316.1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; no longer C277.1, C278.1, C279.1, C280.1, C281.1, C282.1, C283.1, C296.1, R156.2, R157.2, R173.2, R178.2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
- net 5V_A: now also C236.1, C288.1, C293.1, C294.1, R175.2, C315.1, R199.1, U35.5 (V5); no longer C268.1, C273.1, C274.1, C295.1, R162.2, R186.1
- net 5V_C: now also R195.1; no longer R182.1
- net A4_USB2_DN: now also U35.10 (DM1); no longer U33.16 (DM4)
- net A4_USB2_DP: now also U35.9 (DP1); no longer U33.15 (DP4)
- net AGND: now also C292.2; no longer C272.2
- net AMP_INN: now also C292.1; no longer C272.1
- net AMP_INP: now also C290.2, C291.2; no longer C270.2, C271.2
- net AMP_SD#: now also R163.1; no longer R150.1
- net AUD_3V3: now also C284.1, C285.1, R159.2, R160.2; no longer C264.1, C265.1, R146.2, R147.2
- net AUD_AVDD: now also C286.1, C287.1; no longer C266.1, C267.1
- net AUD_OPT_3V3: now also C289.1, R161.2; no longer C269.1, R148.2
- net AUD_XI: now also C282.1; no longer C262.1
- net AUD_XO: now also C283.1; no longer C263.1
- net BK3_FB: now also R202.2, R203.1; no longer R189.2, R190.1
- net BKA_BOOT: now also C310.1; no longer C290.1
- net BKA_FB: now also R199.2, R200.1; no longer R186.2, R187.1
- net BKA_MODE: now also R198.1; no longer R185.1
- net BKA_SS: now also C312.1; no longer C292.1
- net BKA_SW: now also C310.2; no longer C290.2
- net BKA_VREG5: now also C311.1; no longer C291.1
- net BKC_BOOT: now also C307.1; no longer C287.1
- net BKC_FB: now also R195.2, R196.1; no longer R182.2, R183.1
- net BKC_MODE: now also R194.1; no longer R181.1
- net BKC_SS: now also C309.1; no longer C289.1
- net BKC_SW: now also C307.2; no longer C287.2
- net BKC_VREG5: now also C308.1; no longer C288.1
- net DIAG_BTN_N: now also R180.1; no longer R167.1
- net DL_HPD2: now also R155.1; no longer R142.1
- net EFUSE_DVDT: now also C306.1; no longer C286.1
- net EFUSE_EN: now also R187.2, R188.1; no longer R174.2, R175.1
- net EFUSE_FLT#: now also R192.1, R193.1; no longer R179.1, R180.1
- net EFUSE_ILIM: now also R189.1; no longer R176.1
- net EFUSE_IMON: now also R190.1; no longer R177.1
- net EFUSE_PG: now also R191.1; no longer R178.1
- net ETH1_CT: now also C248.1, T1.12 (CCT4), T1.3 (CCT1), T1.6 (CCT2), T1.9 (CCT3); no longer C244.1
- net ETH1_MDI0_N: now also T1.2 (C1-)
- net ETH1_MDI0_P: now also T1.1 (C1+)
- net ETH1_MDI1_N: now also T1.5 (C2-)
- net ETH1_LEDG_A renamed ETH1_LCT0
- net ETH1_LEDY_A renamed ETH1_LCT1
- net ETH2_LEDY_A renamed I226S_RSET
- removed net I226B_0V9: C249.1, C250.1, C251.1, L45.2, U52.18 (VCC0P9)
- net I226B_RSET renamed ETH1_LCT3
- net I226B_SPI_CLK renamed I226S_SPI_CLK
- net I226B_SPI_CS# renamed I226S_SPI_CS#
- net I226B_SPI_MISO renamed I226S_SPI_MISO
- net I226B_SPI_MOSI renamed I226S_SPI_MOSI
- net I226B_SVR renamed I226S_SVR
- net I226B_XI renamed I226S_XI
- net I226B_XO renamed I226S_XO
- net PCIE_I226B_RX_N renamed PCIE_I226S_RX_N
- net PCIE_I226B_RX_P renamed PCIE_I226S_RX_P
- new net 3V3_WL: C273.1, C274.1, C275.1, J7.24 (3V3_WL_24), J7.26 (3V3_WL_26), J7.28 (3V3_WL_28), J7.30 (3V3_WL_30), U92.2
- new net BT_DISABLE#: J7.29 (BT_DISABLE#), R147.1
- new net BT_USB2_DN: J7.20 (BT_USB2_DN), U35.12 (DM2)
- new net BT_USB2_DP: J7.18 (BT_USB2_DP), U35.11 (DP2)
- new net EMC_DN: Q90.2, U90.8 (DN)
- new net EMC_DP: Q90.1, U90.7 (DP)
- new net ETH1_BOB: C249.1, R132.2, R133.2, R134.2, R135.2
- new net ETH1_LCT2: R134.1, T1.21 (LCT3)
- new net ETH1_TRD0_N: J25.2 (P2), T1.14 (L1-)
- new net ETH1_TRD0_P: J25.1 (P1), T1.13 (L1+)
- new net ETH1_TRD1_N: J25.4 (P4), T1.17 (L2-)
- new net ETH1_TRD1_P: J25.3 (P3), T1.16 (L2+)
- new net ETH1_TRD2_N: J25.6 (P6), T1.20 (L3-)
- new net ETH1_TRD2_P: J25.5 (P5), T1.19 (L3+)
- new net ETH1_TRD3_N: J25.8 (P8), T1.23 (L4-)
- new net ETH1_TRD3_P: J25.7 (P7), T1.22 (L4+)
- new net ETH2_BOB: C262.1, R138.2, R139.2, R140.2, R141.2
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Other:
- note added: "CONN_C fan + AirPort (J7), EMC2101 U90, ASM1182e U91 (PCIe x1 shared with i226 #2)"
- note added: "USB2 hubs CH334R (H1a U34, H1b U32, H2 U33, H3 U35)"
- note removed: "USB2 hubs CH334R (H1a U34, H1b U32, H2 U33)"
